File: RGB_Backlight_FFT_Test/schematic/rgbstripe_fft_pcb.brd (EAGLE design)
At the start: 46 x 62.3 mm, 15 parts, among them J1 POWER_JACK, J2 AUDIO_JACK_3.5MM_KIT, M1 ARDUINO-NANO-3.0

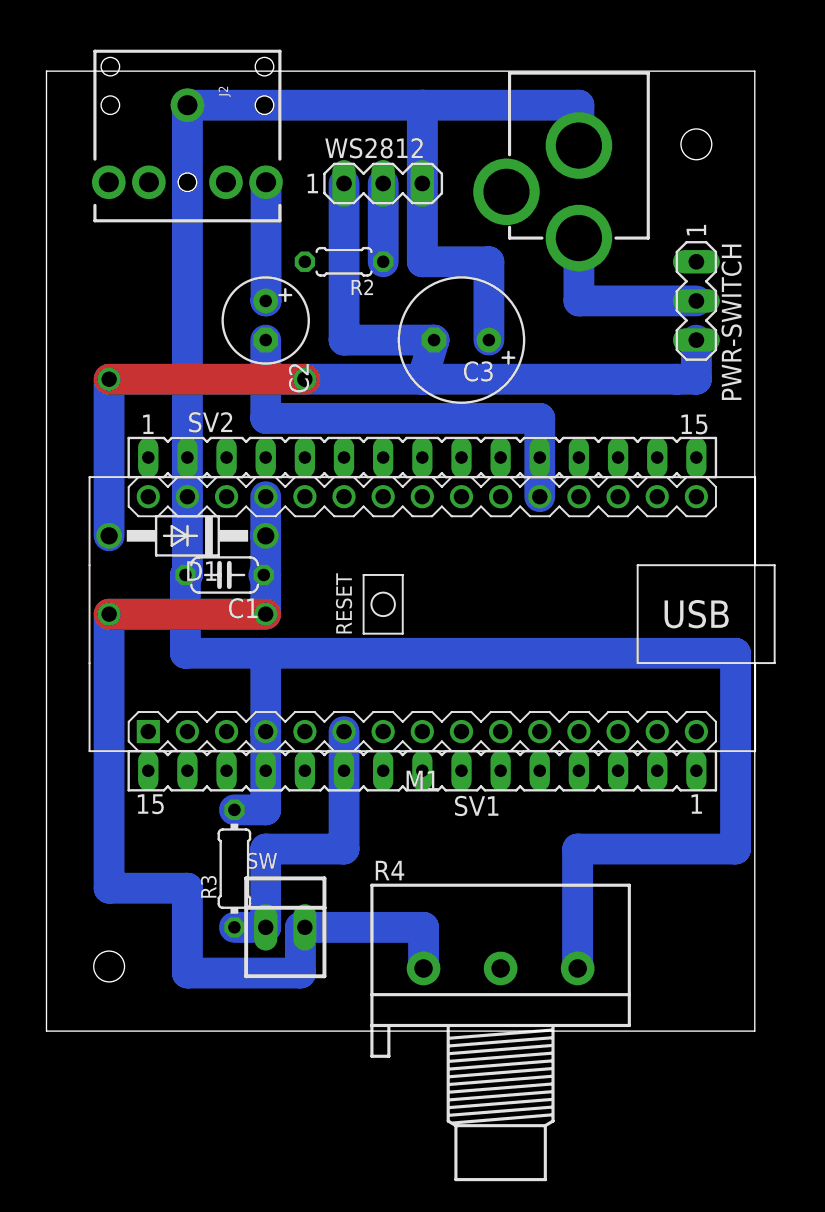
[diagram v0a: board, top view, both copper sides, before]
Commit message: case: 123Design case added + Sketches Updates
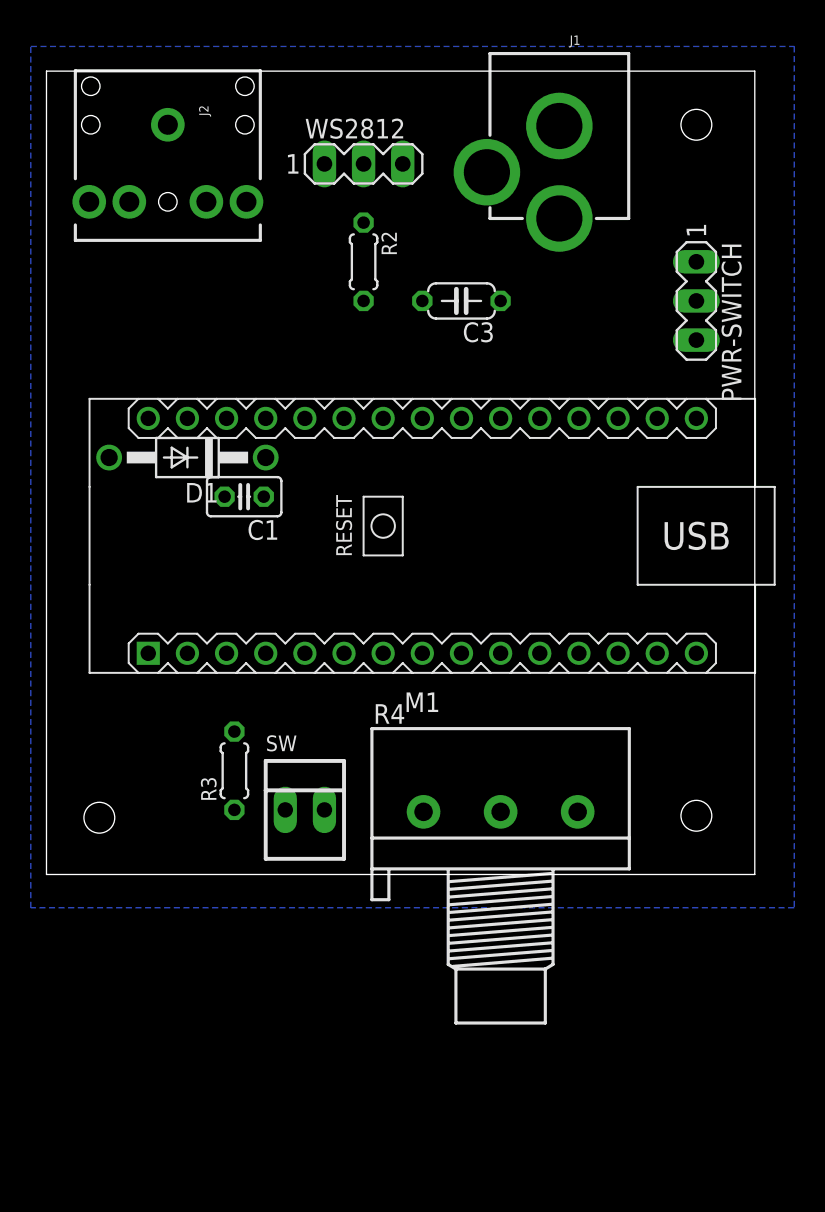
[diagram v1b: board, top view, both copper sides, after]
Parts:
- removed C2: 10uF, resistor:E2,5-6
- removed SV1, SV2: (no value), con-lsta:FE15
- C1: device resistor:C050-024X044 -> resistor:C025-025X050
- C3: device resistor:E3,5-8 -> resistor:C050-024X044
- R3: value 220k -> 10k; device resistor:0204/7 -> resistor:0204/5
- moved R4 10.2 mm to (143.5, 51.9)
- moved SW 7.73 mm to (130.8, 52.1)
- moved R3 6.35 mm to (126.2, 54.6)
- moved C1 5.24 mm to (126.9, 72.4)
- moved D1 5.08 mm to (123.2, 74.9)
- moved M1 5.08 mm to (138.4, 69.8)
- moved C3 2.54 mm to (141.0, 85.1)
- moved J1 1.80 mm to (147.3, 104.1)
- moved J2 1.80 mm to (121.9, 96.5)
- moved WS2812 1.80 mm to (134.6, 94.0)
- moved R2 1.27 mm to (134.6, 87.6), turned to 270 degrees
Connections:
- removed net N$3: C2.+, J2.RING
- net GND: now also C3.1, J1.GNDBREAK; no longer C3.+
- net N$1: no longer R4.1, SW.2
- net N$6: now also J2.RING; no longer C2.-
- net VCC: now also C3.2, R4.1, SW.2; no longer C3.-
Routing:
- net GND: track 161.8 -> 0.00 mm
- net N$1: track 67.2 -> 0.00 mm, vias 1 -> 0
- net VCC: track 56.8 -> 0.00 mm, vias 1 -> 0
- net N$6: track 27.9 -> 0.00 mm
- net N$17: track 19.8 -> 0.00 mm
- net N$2: track 12.7 -> 0.00 mm, vias 1 -> 0
- net N$19: track 11.4 -> 0.00 mm
- net N$3: track 7.72 -> 0.00 mm
- net N$16: track 5.08 -> 0.00 mm
- added copper zone on layer 16, net GND
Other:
- board size 46 x 62.3 mm -> 46 x 52.1 mm
